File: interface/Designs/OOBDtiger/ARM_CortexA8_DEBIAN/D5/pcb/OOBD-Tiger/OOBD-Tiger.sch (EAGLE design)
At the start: 83 parts, among them IC4 DS3231, U1 SY6280, U10 MP1482DS, U2 SN65HVD230(SO8), U6 SN65HVD230(SO8)

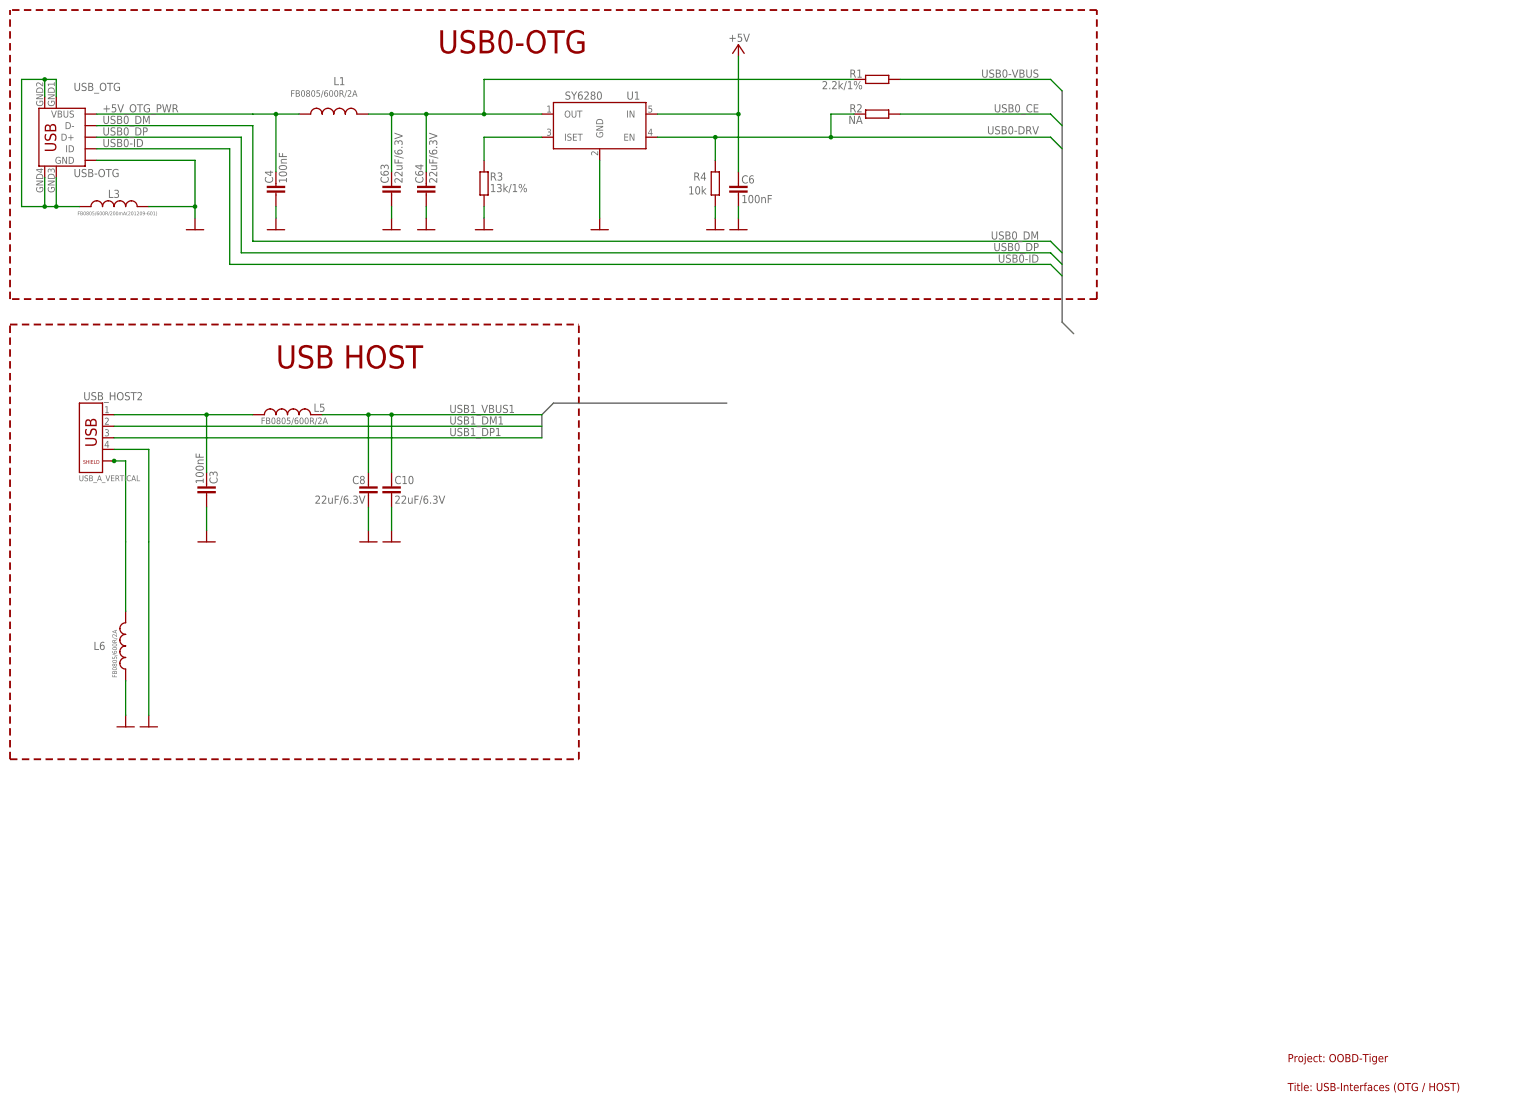
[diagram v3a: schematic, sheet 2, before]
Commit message: modify USB-OTG and USB-Host interface
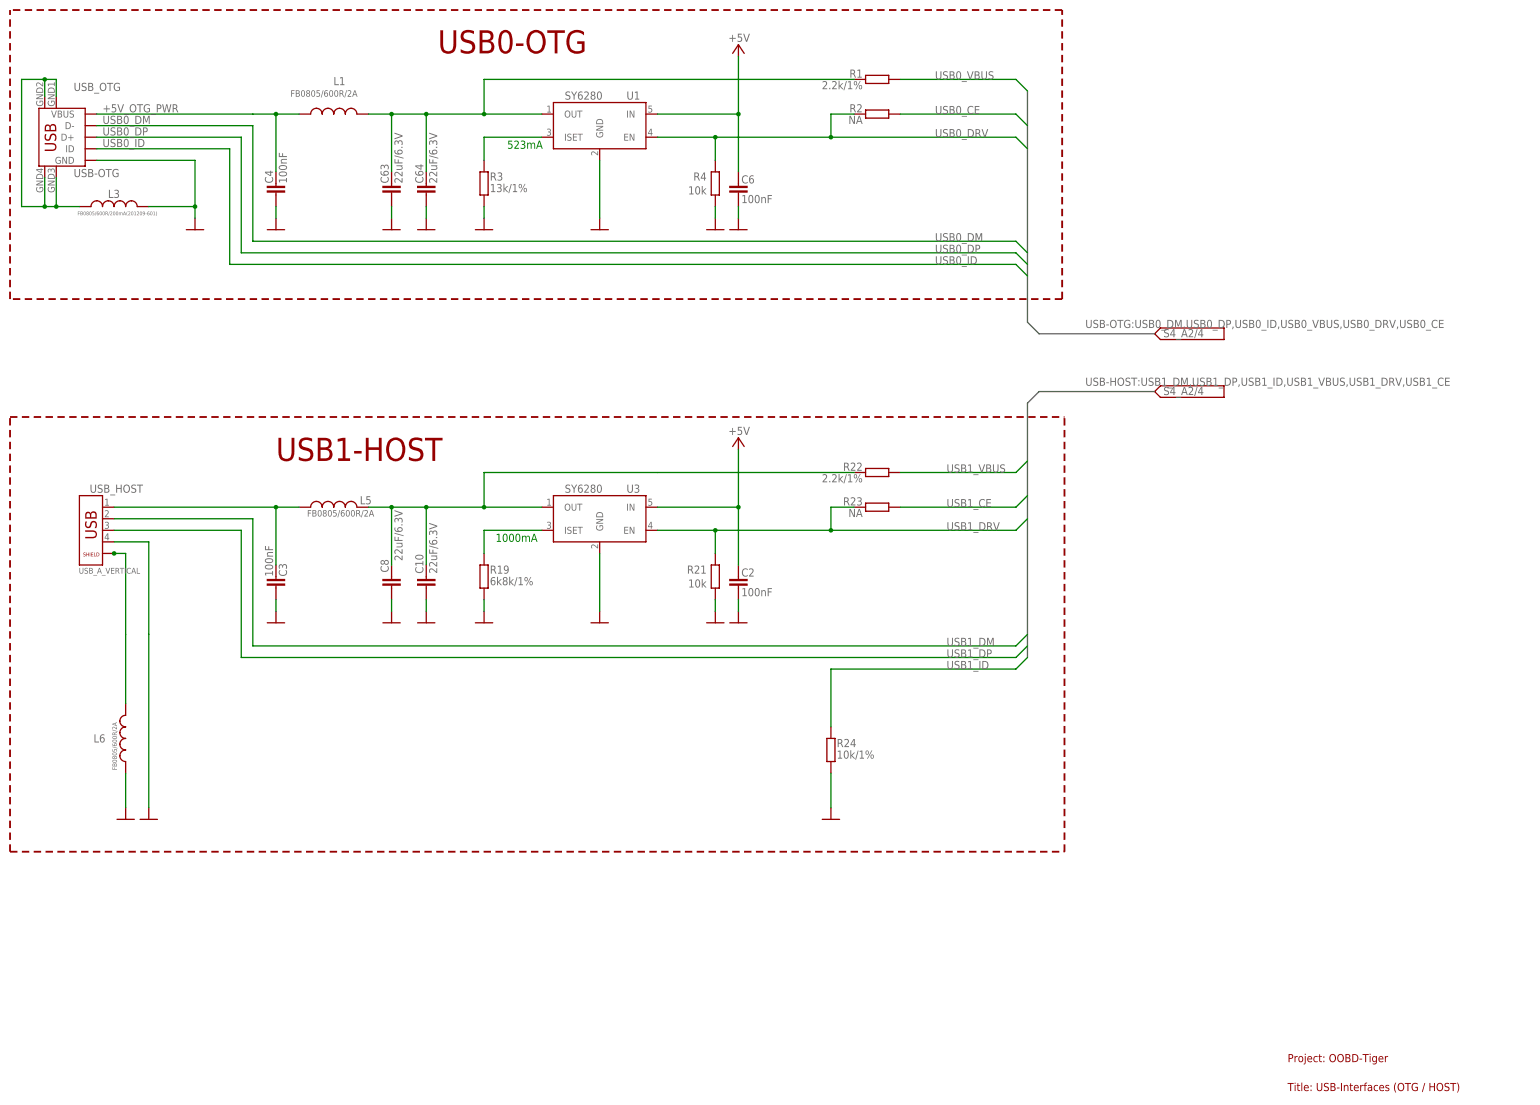
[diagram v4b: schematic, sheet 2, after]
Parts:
- removed USB_HOST2: USB_A_VERTICAL, OLIMEX_CONNECTORS:USB_SHIELD1
- added C2: 100nF, rcl:C-EUC0603
- added R19: 6k8k/1%, rcl:R-EU_R0603
- added R21: 10k, rcl:R-EU_R0603
- added R22: 2.2k/1%, rcl:R-EU_R0603
- added R23: NA, rcl:R-EU_R0603
- added R24: 10k/1%, rcl:R-EU_R0603
- added U3: SY6280, OLIMEX_IC:SY6280
- added USB_HOST: USB_A_VERTICAL, OLIMEX_CONNECTORS:USB_SHIELD1
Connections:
- net USB0-DRV renamed USB0_DRV
- net USB0-ID renamed USB0_ID
- net USB0-VBUS renamed USB0_VBUS
- removed net USB1_DM1: USB_HOST2.2
- removed net USB1_DP1: USB_HOST2.3
- removed net USB1_VBUS1: C10.1, C8.1, L5.1
- new net N$13: C10.1, C8.1, L5.1, R22.2, U3.OUT
- new net N$3: R19.2, U3.ISET
- net +5V: now also C2.1, U3.IN
- net GND: now also C2.2, R19.1, R21.1, R24.1, U3.GND, USB_HOST.4; no longer USB_HOST2.4
- net N$28: now also USB_HOST.1; no longer USB_HOST2.1
- net N$29: now also USB_HOST.5, USB_HOST.6; no longer USB_HOST2.5, USB_HOST2.6
- net USB1_CE: now also R23.2
- net USB1_DM: now also USB_HOST.2
- net USB1_DP: now also USB_HOST.3
- net USB1_DRV: now also R21.2, R23.1, U3.EN
- net USB1_ID: now also R24.2
- net USB1_VBUS: now also R22.1
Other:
- note added: "1000mA"
- note added: "523mA"
- note added: "USB1-HOST"
- note removed: "USB HOST"
- moved on the sheet: C10, C3, C8, L5, L6

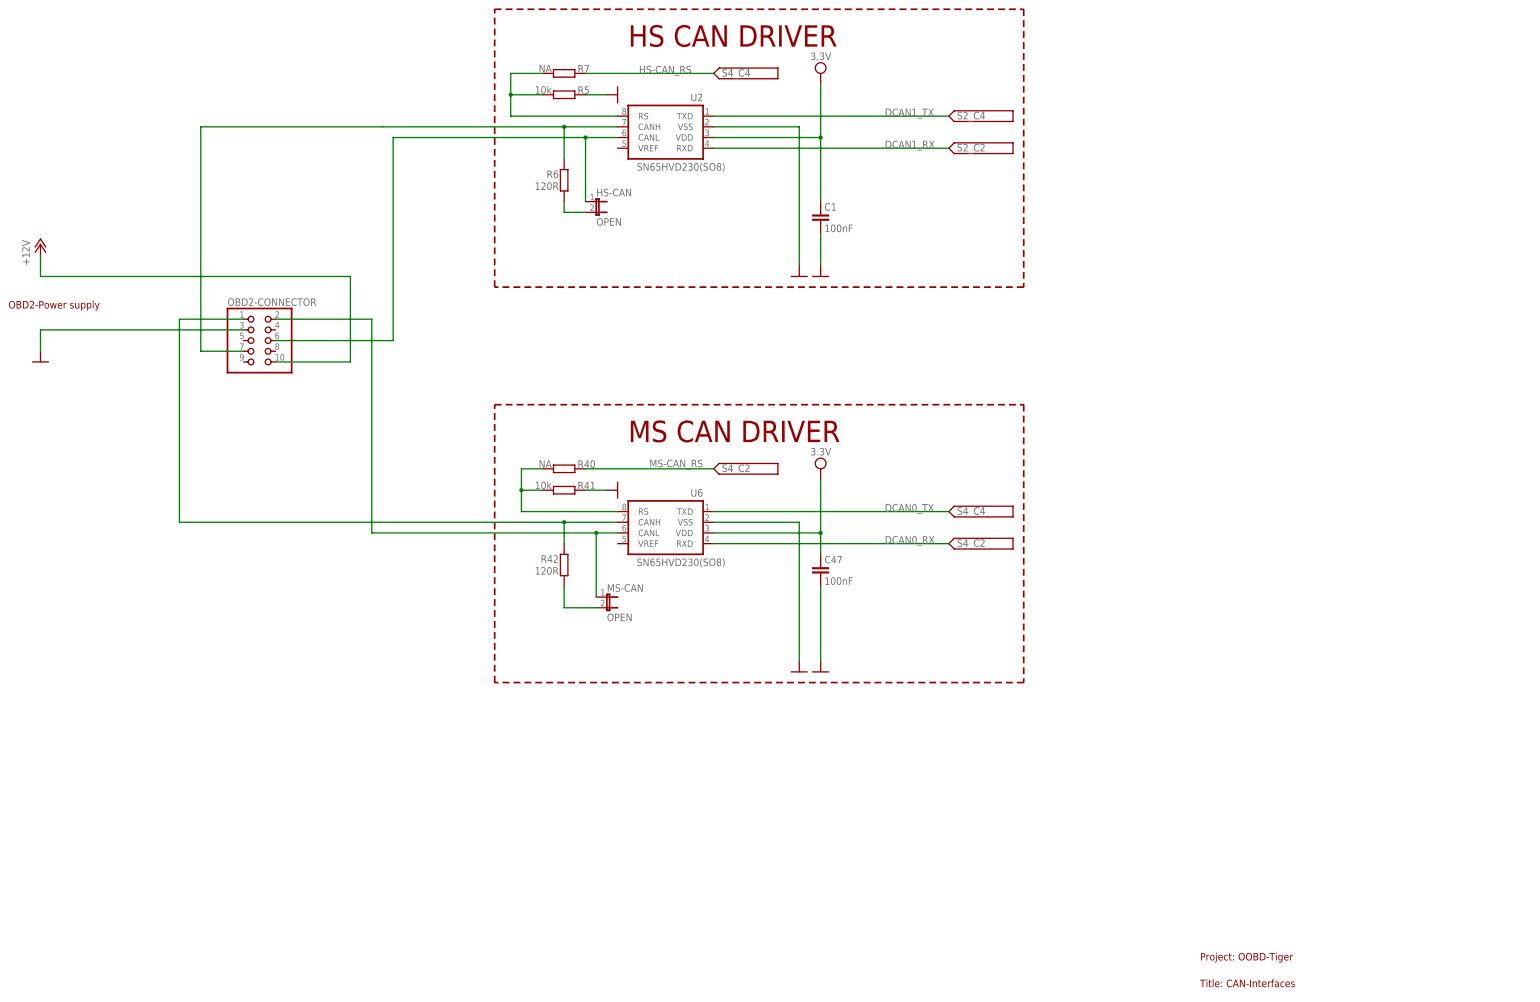
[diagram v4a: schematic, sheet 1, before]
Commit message: ISO1050 wieder entfernt, ADM3053 hinzugefügt, optional als Jumper
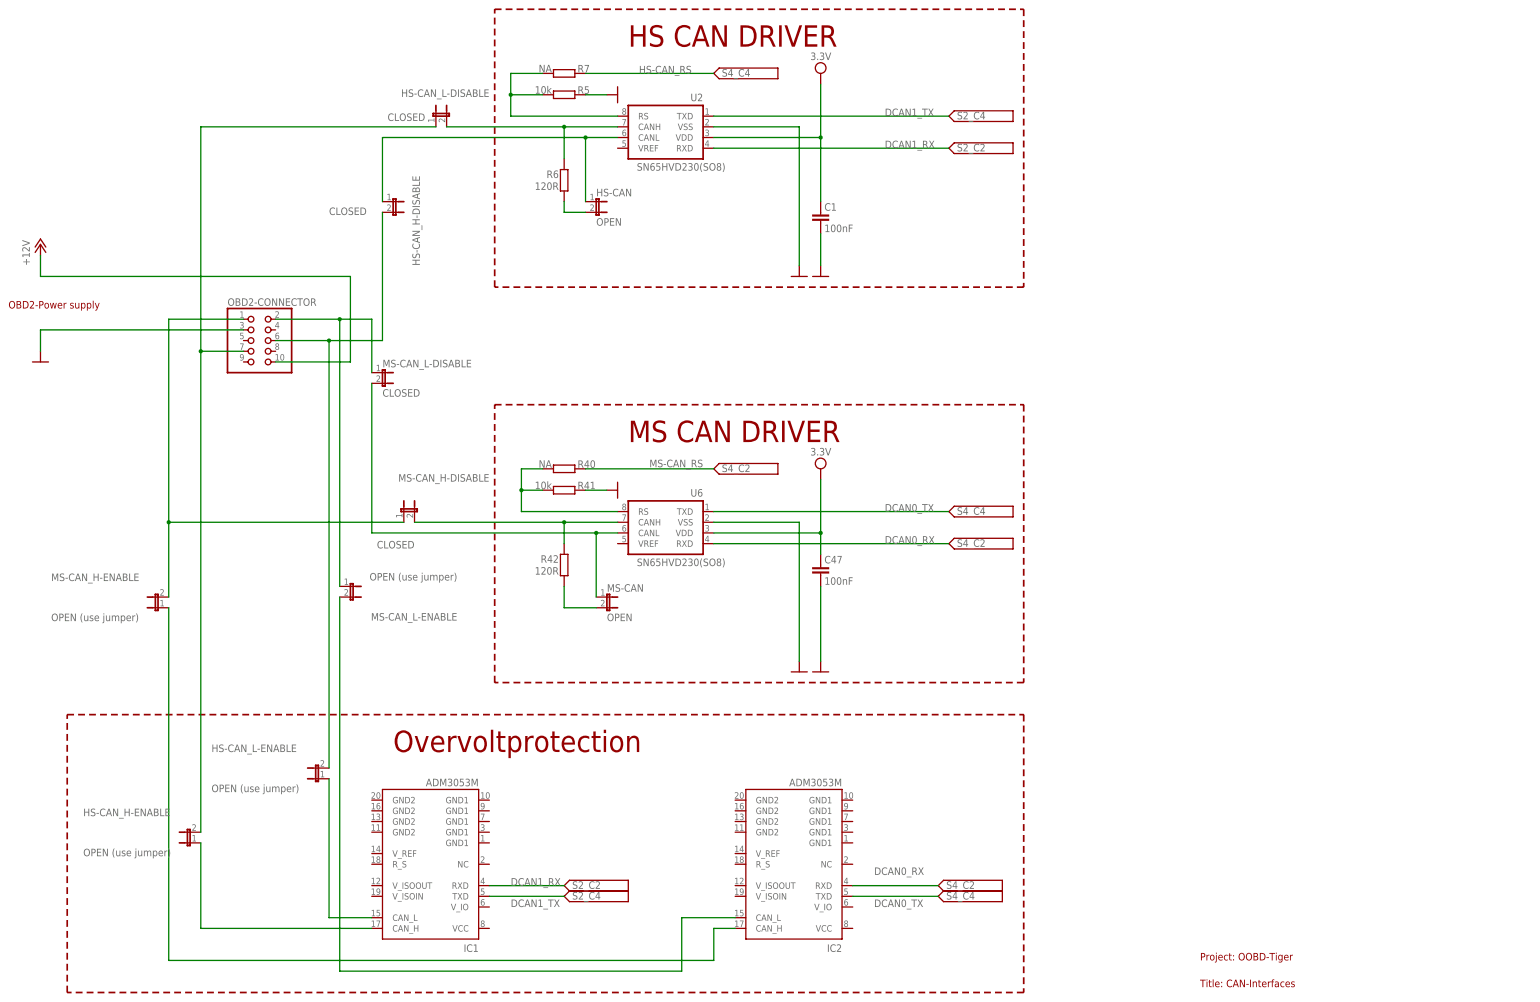
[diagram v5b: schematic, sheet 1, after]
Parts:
- added HS-CAN_H-DISABLE, HS-CAN_L-DISABLE, MS-CAN_H-DISABLE, MS-CAN_L-DISABLE: CLOSED, SparkFun:JUMPER-2SMD-NO
- added HS-CAN_H-ENABLE, HS-CAN_L-ENABLE, MS-CAN_H-ENABLE, MS-CAN_L-ENABLE: OPEN (use jumper), SparkFun:JUMPER-2SMD-NO
- added IC1, IC2: ADM3053M, ADM3053:ADM3053M
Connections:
- new net N$30: HS-CAN_L-DISABLE.2, R6.2, U2.CANH
- new net N$31: HS-CAN_H-DISABLE.2, HS-CAN_L-ENABLE.2, OBD2-CONNECTOR.6
- new net N$32: IC2.CAN_L, MS-CAN_L-ENABLE.2
- new net N$33: MS-CAN_H-DISABLE.2, R42.2, U6.CANH
- new net N$34: HS-CAN_H-ENABLE.1, IC1.CAN_H
- new net N$35: HS-CAN_L-ENABLE.1, IC1.CAN_L
- new net N$36: MS-CAN_L-DISABLE.1, MS-CAN_L-ENABLE.1, OBD2-CONNECTOR.2
- new net N$37: MS-CAN_H-DISABLE.1, MS-CAN_H-ENABLE.2, OBD2-CONNECTOR.1
- net CANH: now also IC2.CAN_H, MS-CAN_H-ENABLE.1; no longer OBD2-CONNECTOR.1, R42.2, U6.CANH
- net CANH1: now also HS-CAN_H-ENABLE.2, HS-CAN_L-DISABLE.1; no longer R6.2, U2.CANH
- net CANL: now also MS-CAN_L-DISABLE.2; no longer OBD2-CONNECTOR.2
- net CANL1: now also HS-CAN_H-DISABLE.1; no longer OBD2-CONNECTOR.6
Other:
- note added: "Overvoltprotection"

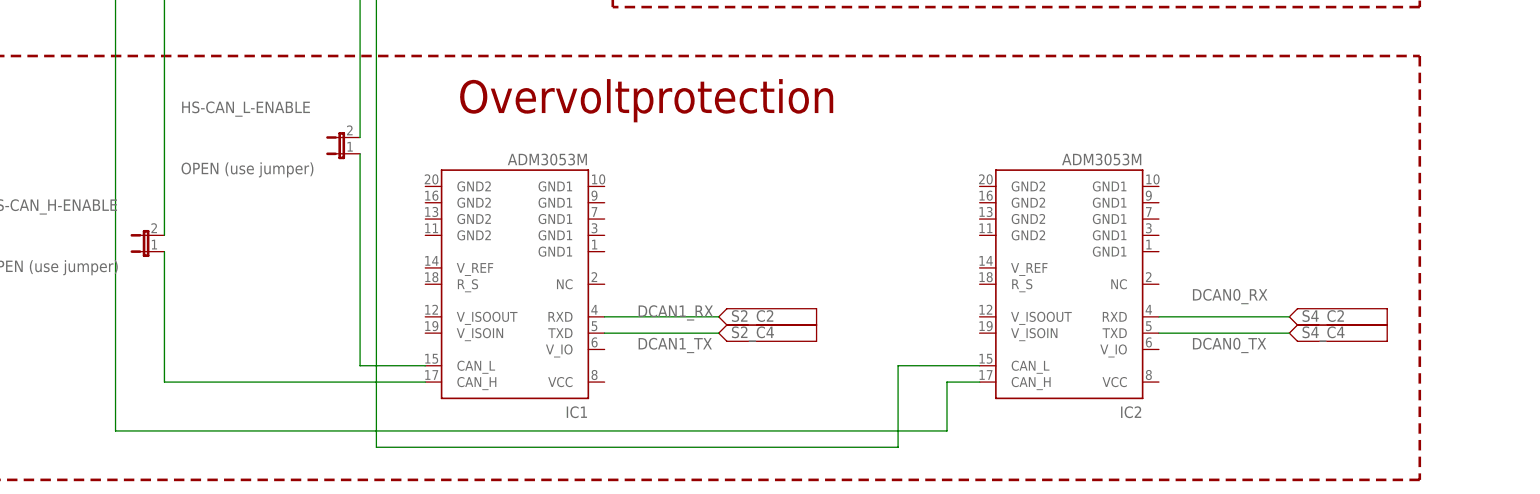
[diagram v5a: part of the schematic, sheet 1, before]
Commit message: ADM3053 mit Beschallung gesehen und auf dem PCB platziert.
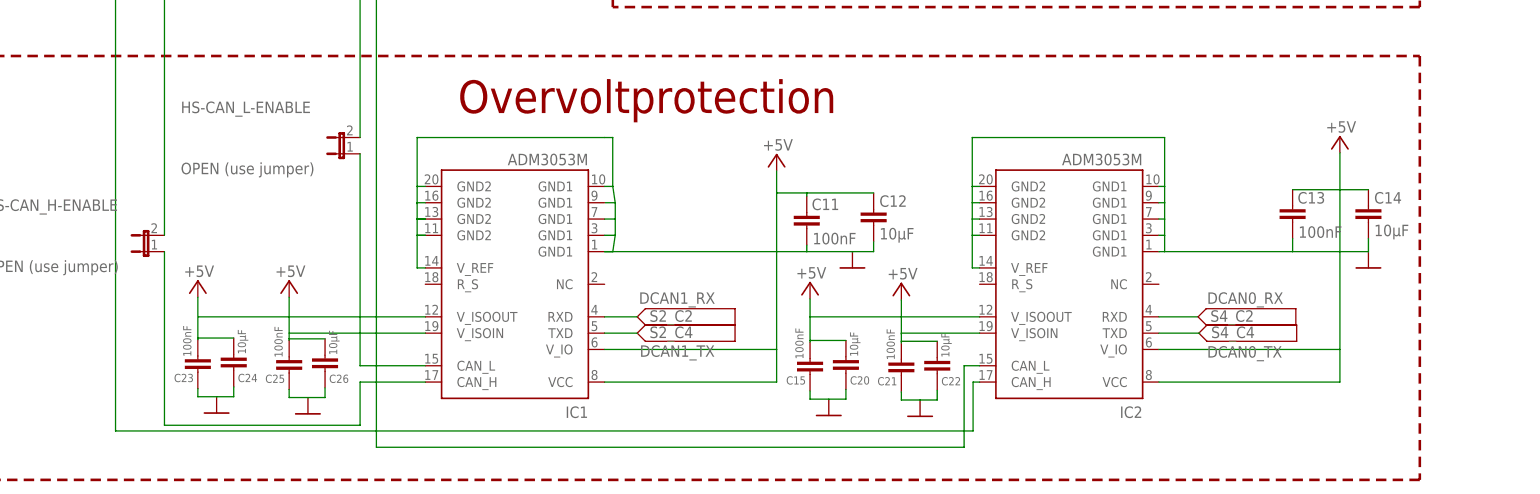
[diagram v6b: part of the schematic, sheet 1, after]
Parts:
- added C11, C13, C15, C21, C23, C25: 100nF, rcl:C-EU2
- added C12, C14, C20, C22, C24, C26: 10µF, rcl:C-EU2
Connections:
- new net N$38: IC2.GND2@0, IC2.GND2@1, IC2.GND2@2, IC2.V_REF
- new net N$39: IC2.V_IO
- new net N$40: IC1.V_ISOIN
- new net N$41: IC1.V_ISOOUT
- new net N$42: IC2.GND1@3, IC2.GND1@4, IC2.GND2@3
- new net N$45: IC1.GND2@0, IC1.GND2@1, IC1.GND2@2, IC1.V_REF
- new net N$46: IC1.GND1@4, IC1.GND2@3
- net +5V: now also C11.1, C12.1, C13.1, C14.1, C15.1, C20.1, C21.1, C22.1, C23.1, C24.1, C25.1, C26.1, IC1.VCC, IC1.V_IO, IC2.VCC, IC2.V_ISOIN, IC2.V_ISOOUT
- net GND: now also C11.2, C12.2, C13.2, C14.2, C15.2, C20.2, C21.2, C22.2, C23.2, C24.2, C25.2, C26.2, IC1.GND1@0, IC1.GND1@1, IC1.GND1@2, IC2.GND1@0, IC2.GND1@1, IC2.GND1@2
